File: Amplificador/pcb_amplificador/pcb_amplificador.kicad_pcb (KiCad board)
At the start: 2 copper layers, 149.9 x 88.9 mm, 139 parts, among them CON1 SJ-3523-SMT-TR, J1 Screw_Terminal_01x02, J2 Screw_Terminal_01x02, J3 Screw_Terminal_01x02, J4 Screw_Terminal_01x02, J5 Conn_01x03_Male, J6 Screw_Terminal_01x02, J7 Screw_Terminal_01x02, K1 FINDER-40.11-2016, M1 FDS9934C, M2 FDS9934C, Q1 BC860, Q10 BD139, Q11 BD140, Q12 BD139, Q13 2SA1943-O_Q_, Q14 2SC5200-O_Q, Q15 2SA1943-O_Q_, Q16 2SC5200-O_Q, Q17 2SAR514P5, Q18 BC860, Q19 BC860, Q2 BC860, Q20 2SAR514P5, Q21 2SCR514P5, Q22 2SCR514P5, Q23 2SCR514P5, Q24 2SAR514P5, Q25 2SCR514P5, Q26 BC817, Q27 BC817, Q28 BC807, Q29 BS170, Q3 BC850, Q4 BC850, Q5 BC860, Q6 BC860, Q7 BC850, Q8 2SCR514P5, Q9 2SCR514P5

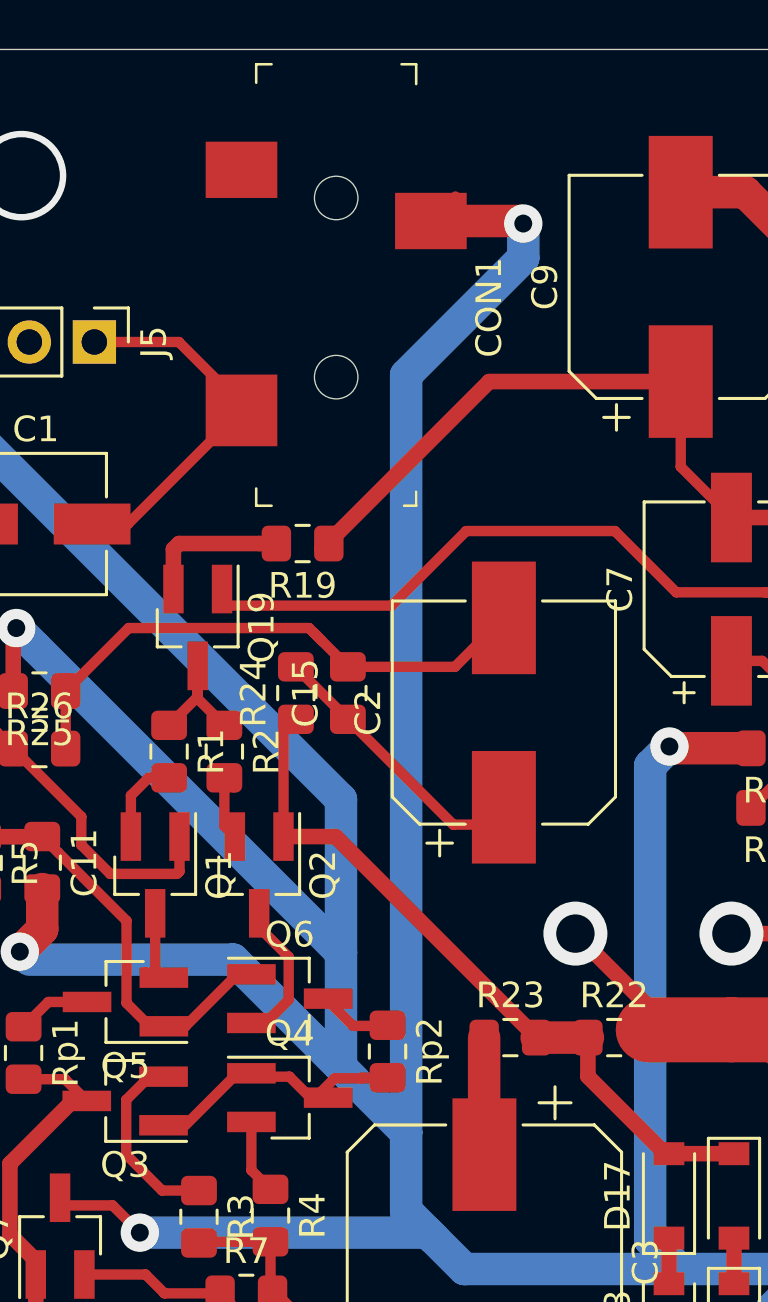
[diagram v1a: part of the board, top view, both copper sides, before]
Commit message: Actualización de las especificaciones del amplificador
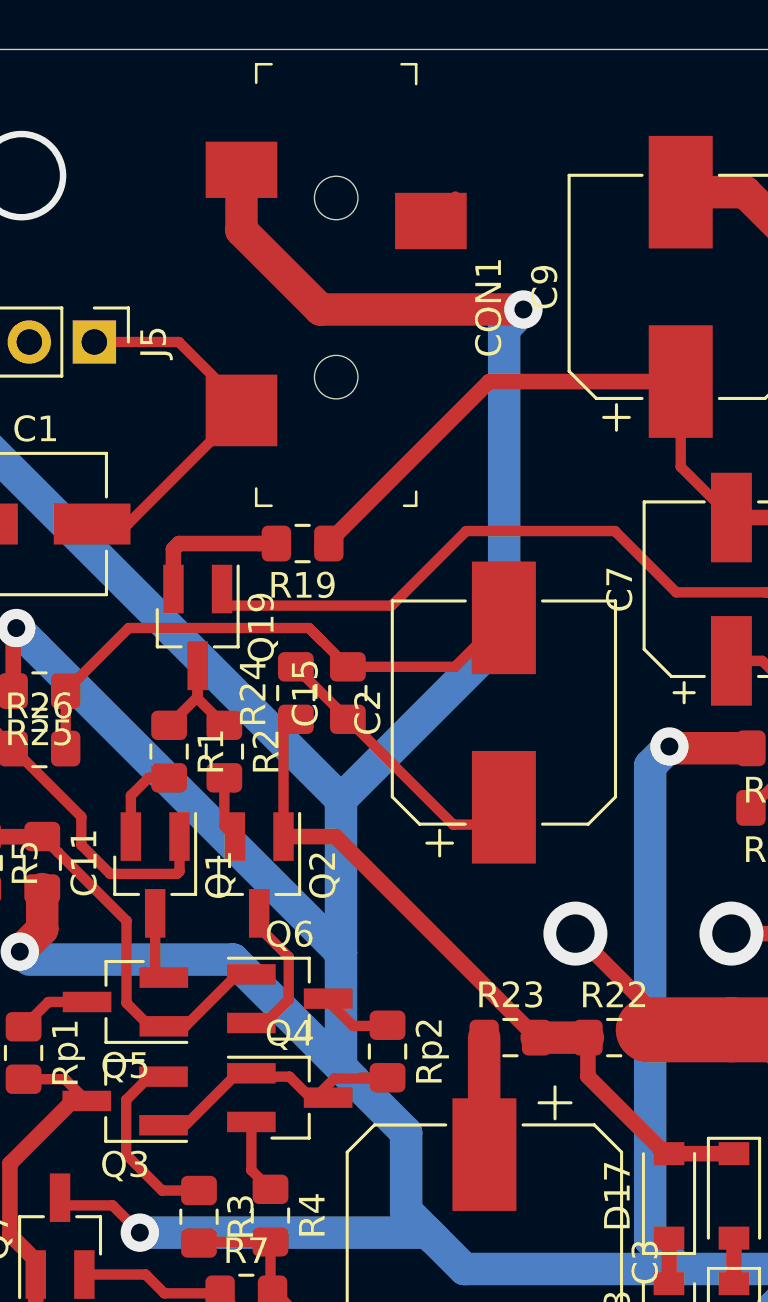
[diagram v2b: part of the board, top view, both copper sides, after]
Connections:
- CON1 pad 1: Net-(CON1-Pad1) -> Earth
- CON1 pad 3: Earth -> Net-(CON1-Pad3)
- J4 pad 2: Net-(J4-Pad1) -> Net-(J4-Pad2)
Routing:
- net Earth: track 607.9 -> 603.1 mm
- net Net-(CON1-Pad3): track 0.00 -> 1.35 mm
- net Net-(CON1-Pad1): track 0.85 -> 0.00 mm
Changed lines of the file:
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@@
     (thickness 1.6)
     (drawings 4)
-    (tracks 1073)
+    (tracks 1075)
     (zones 0)
     (modules 139)
-    (nets 85)
+    (nets 86)
   )
   (page A4)
@@
   )
   (setup
-    (last_trace_width 0.4064)
+    (last_trace_width 1.27)
     (user_trace_width 0.3048)
     (user_trace_width 0.4064)
@@
   (net 79 "Net-(K1-Pad14)")
   (net 80 "Net-(K1-PadA2)")
-  (net 81 "Net-(CON1-Pad1)")
-  (net 82 "Net-(J5-Pad2)")
-  (net 83 "Net-(C18-Pad2)")
-  (net 84 "Net-(K1-Pad11)")
+  (net 81 "Net-(J5-Pad2)")
+  (net 82 "Net-(C18-Pad2)")
+  (net 83 "Net-(K1-Pad11)")
+  (net 84 "Net-(CON1-Pad3)")
+  (net 85 "Net-(J4-Pad2)")
   (net_class Default "This is the default net class."
     (clearance 0.3048)
@@
     (add_net "Net-(C7-Pad1)")
     (add_net "Net-(C7-Pad2)")
-    (add_net "Net-(CON1-Pad1)")
+    (add_net "Net-(CON1-Pad3)")
     (add_net "Net-(D10-Pad1)")
     (add_net "Net-(D10-Pad2)")
@@
     (add_net "Net-(D9-Pad2)")
     (add_net "Net-(J4-Pad1)")
+    (add_net "Net-(J4-Pad2)")
     (add_net "Net-(J5-Pad2)")
     (add_net "Net-(K1-Pad11)")
@@
       (net 79 "Net-(K1-Pad14)"))
     (pad 11 thru_hole circle (at 20.32 7.62 270) (size 3 3) (drill 1.3) (layers *.Cu *.Mask)
-      (net 84 "Net-(K1-Pad11)"))
+      (net 83 "Net-(K1-Pad11)"))
     (pad 12 thru_hole circle (at 15.32 0 270) (size 3 3) (drill 1.3) (layers *.Cu *.Mask)
       (net 71 /VOUT))
@@
       (net 79 "Net-(K1-Pad14)"))
     (pad 11 thru_hole circle (at 20.32 0 270) (size 3 3) (drill 1.3) (layers *.Cu *.Mask)
-      (net 84 "Net-(K1-Pad11)"))
+      (net 83 "Net-(K1-Pad11)"))
     (pad A2 thru_hole circle (at 0 7.62 270) (size 3 3) (drill 1.3) (layers *.Cu *.Mask)
       (net 80 "Net-(K1-PadA2)"))
@@
       (net 1 "Net-(C1-Pad2)"))
     (pad 1 smd rect (at -2 3.7 270) (size 2.2 2.8) (layers F.Cu F.Paste F.Mask)
-      (net 81 "Net-(CON1-Pad1)"))
-    (pad 3 smd rect (at 0 -3.7 270) (size 2.2 2.8) (layers F.Cu F.Paste F.Mask)
       (net 3 Earth))
+    (pad 3 smd rect (at 0 -3.7 270) (size 2.2 2.8) (layers F.Cu F.Paste F.Mask)
+      (net 84 "Net-(CON1-Pad3)"))
   )
   (module Capacitor_SMD:CP_Elec_10x10.5 (layer F.Cu)
@@
     (fp_arc (start 0 3.95) (end -0.75 2.25) (angle 47.6) (layer F.SilkS) (width 0.12))
     (pad 2 thru_hole oval (at 3.5 0) (size 1.8 3.6) (drill 1.2) (layers *.Cu *.Mask)
-      (net 74 "Net-(J4-Pad1)"))
+      (net 85 "Net-(J4-Pad2)"))
     (pad 1 thru_hole roundrect (at 0 0) (size 1.8 3.6) (drill 1.2) (layers *.Cu *.Mask) (roundrect_rratio 0.138889)
       (net 74 "Net-(J4-Pad1)"))
@@
       (net 3 Earth))
     (pad 2 thru_hole oval (at 0 2.54 270) (size 1.7 1.7) (drill 1) (layers *.Cu *.Mask)
-      (net 82 "Net-(J5-Pad2)"))
+      (net 81 "Net-(J5-Pad2)"))
     (pad 1 thru_hole rect (at 0 0 270) (size 1.7 1.7) (drill 1) (layers *.Cu *.Mask)
       (net 1 "Net-(C1-Pad2)"))
@@
     (fp_line (start 0.47 -2.85) (end 0.47 2.85) (layer F.Fab) (width 0.1))
     (pad 2 thru_hole oval (at 15.24 0 90) (size 2.8 2.8) (drill 1.4) (layers *.Cu *.Mask)
-      (net 84 "Net-(K1-Pad11)"))
+      (net 83 "Net-(K1-Pad11)"))
     (pad 1 thru_hole circle (at 0 0 90) (size 2.8 2.8) (drill 1.4) (layers *.Cu *.Mask)
-      (net 83 "Net-(C18-Pad2)"))
+      (net 82 "Net-(C18-Pad2)"))
     (model ${KISYS3DMOD}/Resistor_THT.3dshapes/R_Axial_DIN0614_L14.3mm_D5.7mm_P15.24mm_Horizontal.wrl
       (at (xyz 0 0 0))
@@
     (fp_line (start 0.66 -1.25) (end 0.66 1.25) (layer F.Fab) (width 0.1))
     (pad 2 thru_hole oval (at 7.62 0 180) (size 1.6 1.6) (drill 0.8) (layers *.Cu *.Mask)
-      (net 84 "Net-(K1-Pad11)"))
+      (net 83 "Net-(K1-Pad11)"))
     (pad 1 thru_hole circle (at 0 0 180) (size 1.6 1.6) (drill 0.8) (layers *.Cu *.Mask)
       (net 74 "Net-(J4-Pad1)"))
@@
     (fp_line (start 0 -2.5) (end 0 2.5) (layer F.Fab) (width 0.1))
     (pad 2 thru_hole circle (at 7.5 0) (size 2 2) (drill 1) (layers *.Cu *.Mask)
-      (net 83 "Net-(C18-Pad2)"))
+      (net 82 "Net-(C18-Pad2)"))
     (pad 1 thru_hole circle (at 0 0) (size 2 2) (drill 1) (layers *.Cu *.Mask)
       (net 3 Earth))
@@
   (via (at 131.699 65.151) (size 1.5) (drill 0.70104) (layers F.Cu B.Cu) (net 3))
   (segment (start 143.972165 55.950573) (end 144.047165 55.875573) (width 0.4064) (layer F.Cu) (net 3))
-  (via (at 54.60492 58.87212) (size 1.5) (drill 0.70104) (layers F.Cu B.Cu) (net 3))
   (segment (start 136.157165 62.930573) (end 136.078427 62.930573) (width 0.4064) (layer F.Cu) (net 3))
-  (segment (start 50.995703 58.772487) (end 51.9527 57.81549) (width 0.4064) (layer F.Cu) (net 3))
+  (segment (start 50.995703 58.772487) (end 51.9527 57.81549) (width 0.4064) (layer F.Cu) (net 84))
   (segment (start 72.136 101.092) (end 72.136 97.592) (width 3.81) (layer B.Cu) (net 3))
   (segment (start 72.136 101.092) (end 68.160199 105.067801) (width 3.81) (layer B.Cu) (net 3))
@@
   (segment (start 65.8622 66.41084) (end 65.8622 99.7204) (width 1.27) (layer B.Cu) (net 3))
   (segment (start 66.76136 65.51168) (end 65.8622 66.41084) (width 1.27) (layer B.Cu) (net 3))
-  (segment (start 54.505287 58.772487) (end 54.60492 58.87212) (width 1.27) (layer F.Cu) (net 3))
-  (segment (start 50.995703 58.772487) (end 54.505287 58.772487) (width 1.27) (layer F.Cu) (net 3))
-  (segment (start 54.60492 60.212176) (end 50.02784 64.789256) (width 1.27) (layer B.Cu) (net 3))
-  (segment (start 54.60492 58.87212) (end 54.60492 60.212176) (width 1.27) (layer B.Cu) (net 3))
   (via (at 39.624 98.298) (size 1.5) (drill 0.70104) (layers F.Cu B.Cu) (net 3))
   (via (at 34.935 87.32) (size 1.5) (drill 0.70104) (layers F.Cu B.Cu) (net 3))
@@
   (segment (start 32.75076 66.63944) (end 32.75076 66.63944) (width 1.27) (layer F.Cu) (net 3))
   (via (at 32.75076 66.63944) (size 1.5) (drill 0.70104) (layers F.Cu B.Cu) (net 3))
-  (segment (start 50.02784 64.789256) (end 50.02784 94.3864) (width 1.27) (layer B.Cu) (net 3))
   (segment (start 50.02784 94.3864) (end 50.02784 97.44456) (width 1.27) (layer B.Cu) (net 3))
   (segment (start 60.38088 79.36992) (end 60.31484 79.30388) (width 1.27) (layer F.Cu) (net 3))
@@
   (segment (start 145.878679 73.160761) (end 148.418679 73.160761) (width 0.4064) (layer F.Cu) (net 80))
   (segment (start 144.37868 74.66076) (end 145.878679 73.160761) (width 0.4064) (layer F.Cu) (net 80))
-  (segment (start 42.992703 57.375487) (end 43.595703 56.772487) (width 0.4064) (layer F.Cu) (net 81))
-  (segment (start 158.53664 112.23752) (end 155.88996 109.59084) (width 3.81) (layer B.Cu) (net 83))
-  (segment (start 155.74772 109.73308) (end 153.52968 109.73308) (width 3.81) (layer B.Cu) (net 83))
-  (segment (start 155.88996 109.59084) (end 155.74772 109.73308) (width 3.81) (layer B.Cu) (net 83))
-  (segment (start 144.4244 94.93504) (end 144.37868 94.98076) (width 3.81) (layer B.Cu) (net 84))
-  (segment (start 156.51988 94.98076) (end 158.53664 96.99752) (width 3.81) (layer B.Cu) (net 84))
-  (segment (start 151.99868 94.98076) (end 156.51988 94.98076) (width 3.81) (layer B.Cu) (net 84))
-  (segment (start 156.51988 94.56928) (end 158.0896 92.99956) (width 3.81) (layer B.Cu) (net 84))
-  (segment (start 156.51988 94.98076) (end 156.51988 94.56928) (width 3.81) (layer B.Cu) (net 84))
-  (segment (start 151.99868 94.98076) (end 144.37868 94.98076) (width 3.81) (layer B.Cu) (net 84))
+  (segment (start 42.992703 57.375487) (end 43.595703 56.772487) (width 0.4064) (layer F.Cu) (net 3))
+  (segment (start 43.595703 59.142487) (end 46.683216 62.23) (width 1.27) (layer F.Cu) (net 3))
+  (segment (start 43.595703 56.772487) (end 43.595703 59.142487) (width 1.27) (layer F.Cu) (net 3))
+  (segment (start 46.683216 62.23) (end 54.61 62.23) (width 1.27) (layer F.Cu) (net 3))
+  (segment (start 54.61 62.23) (end 54.61 62.23) (width 1.27) (layer F.Cu) (net 3))
+  (via (at 54.61 62.23) (size 1.5) (drill 0.7) (layers F.Cu B.Cu) (net 3))
+  (segment (start 53.860001 74.994199) (end 47.48276 81.37144) (width 1.27) (layer B.Cu) (net 3))
+  (segment (start 53.860001 62.979999) (end 53.860001 74.994199) (width 1.27) (layer B.Cu) (net 3))
+  (segment (start 54.61 62.23) (end 53.860001 62.979999) (width 1.27) (layer B.Cu) (net 3))
+  (segment (start 158.53664 112.23752) (end 155.88996 109.59084) (width 3.81) (layer B.Cu) (net 82))
+  (segment (start 155.74772 109.73308) (end 153.52968 109.73308) (width 3.81) (layer B.Cu) (net 82))
+  (segment (start 155.88996 109.59084) (end 155.74772 109.73308) (width 3.81) (layer B.Cu) (net 82))
+  (segment (start 144.4244 94.93504) (end 144.37868 94.98076) (width 3.81) (layer B.Cu) (net 83))
+  (segment (start 156.51988 94.98076) (end 158.53664 96.99752) (width 3.81) (layer B.Cu) (net 83))
+  (segment (start 151.99868 94.98076) (end 156.51988 94.98076) (width 3.81) (layer B.Cu) (net 83))
+  (segment (start 156.51988 94.56928) (end 158.0896 92.99956) (width 3.81) (layer B.Cu) (net 83))
+  (segment (start 156.51988 94.98076) (end 156.51988 94.56928) (width 3.81) (layer B.Cu) (net 83))
+  (segment (start 151.99868 94.98076) (end 144.37868 94.98076) (width 3.81) (layer B.Cu) (net 83))
 )
